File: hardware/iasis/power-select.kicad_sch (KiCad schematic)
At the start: 23 parts, among them Q1911 2N7002, Q1912 2N7002, U1901 AP22653W6-7, U1902 TPS259470LRPWR

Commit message: Wire the schematic islands and side-match the RP2354 GPIOs
Each sheet now draws its circuits with wires. Labels remain at block edges
and on single-part islands: buttons, test points, decoupling and pull
resistors. The target-port page wires its hierarchical labels straight to
the child sheet pins, the ports page points its labels away from each
block, and the root sheet keeps every block clear of the title block.

The RP2354B GPIOs are reassigned so each signal leaves the package on the
side facing its destination. Update PCB from Schematic applied the 43
U1101 pad-net changes with no geometry change. Otherwise the netlist
matches the previous design, ERC keeps its 14 existing warnings and DRC
reports no parity issues.
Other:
- moved on the sheet: C1903, C1904, C1905, C1906, C1911, C1912, C1913, Q1911, Q1912, R1906, R1907, R1908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

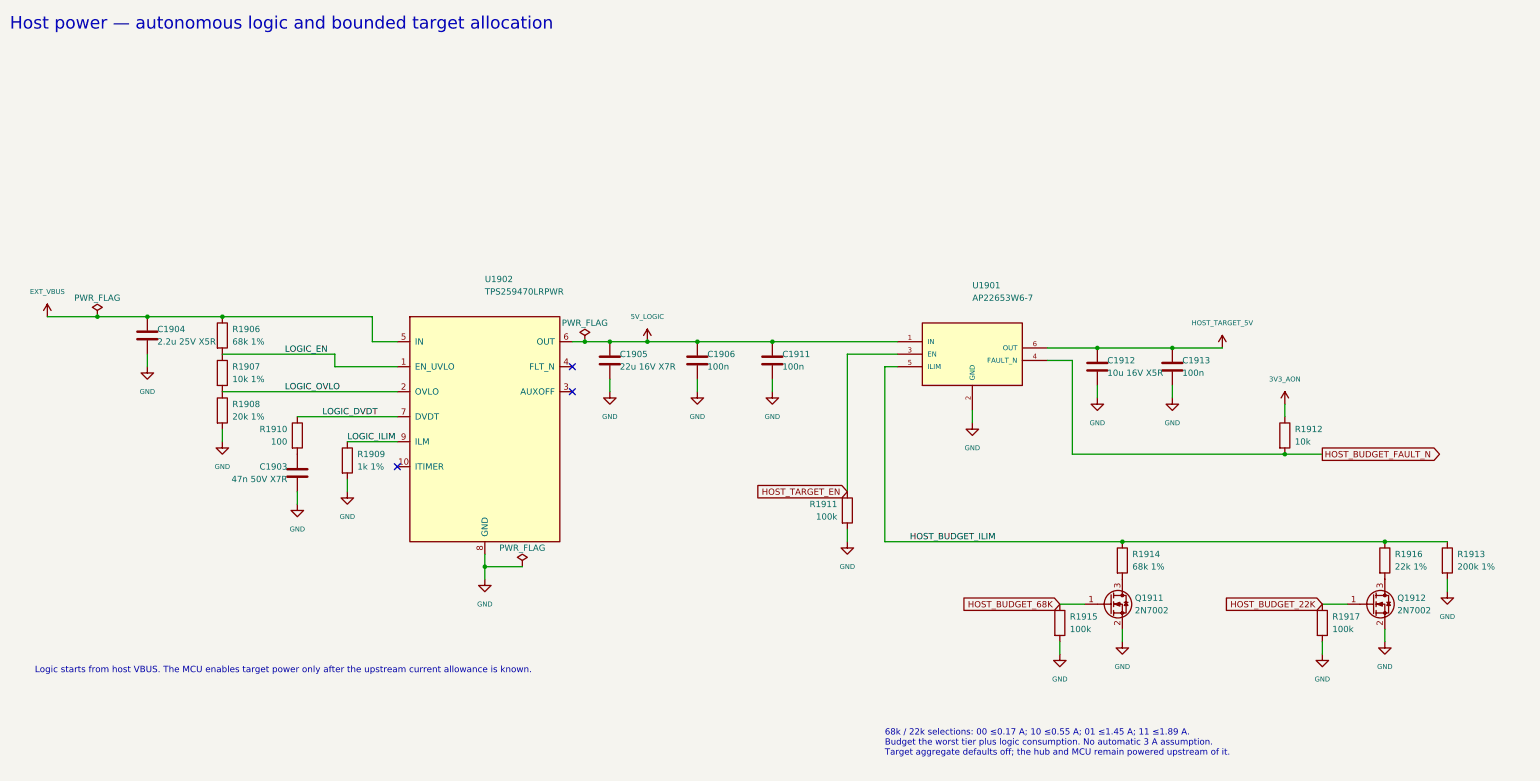
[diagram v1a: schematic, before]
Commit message: Redraw the power input, host power and logic supply sheets
The charging input, host power budget and logic supply sheets follow
the power path left to right: connector and protection, switches and
eFuses, then the converters with their feedback and output capacitors.
Supply rails use power symbols with their existing net names, notes sit
beside their circuits, and each sheet carries a title, date and
revision. The netlist is unchanged.
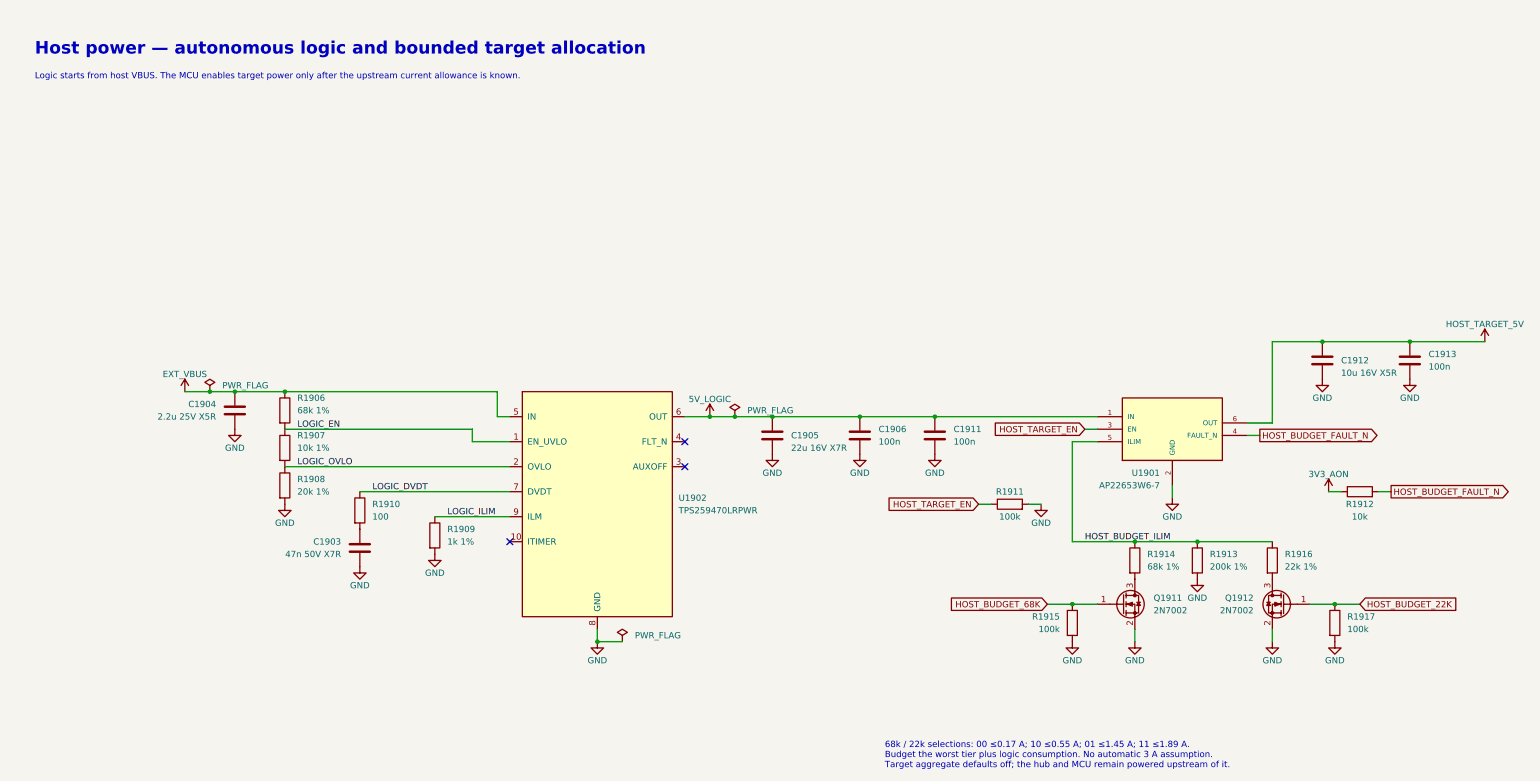
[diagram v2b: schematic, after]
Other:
- title: (none) -> Host power and target budget
- moved on the sheet: C1903, C1904, C1905, C1906, C1911, C1912, C1913, Q1911, Q1912, R1906, R1907, R1908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

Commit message: fix: correct core power and recovery circuitry
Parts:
- R1906: value 68k 1% -> 64.9k 0.1%; LCSC C36871 -> C852880; MPN 0402WGF6802TCE -> RT0402BRD0764K9L; Manufacturer UNI-ROYAL(Uniroyal Elec) -> YAGEO
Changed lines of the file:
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@@
 			)
 		)
-		(property "Value" "68k 1%"
+		(property "Value" "64.9k 0.1%"
 			(at 78.74 95.25 0)
 			(show_name no)
@@
 			)
 		)
-		(property "Datasheet" "https://www.lcsc.com/datasheet/lcsc_datasheet_2206010030_UNI-ROYAL-Uniroyal-Elec-0402WGF6802TCE_C36871.pdf"
+		(property "Datasheet" "https://www.yageogroup.com/component-documentation/download/specsheet/RT0402BRD0764K9L"
 			(at 78.74 95.25 0)
 			(hide yes)
@@
 			)
 		)
-		(property "LCSC" "C36871"
+		(property "LCSC" "C852880"
 			(at 76.2 95.25 0)
 			(hide yes)
@@
 			)
 		)
-		(property "MPN" "0402WGF6802TCE"
+		(property "MPN" "RT0402BRD0764K9L"
 			(at 76.2 95.25 0)
 			(hide yes)
@@
 			)
 		)
-		(property "Manufacturer" "UNI-ROYAL(Uniroyal Elec)"
+		(property "Manufacturer" "YAGEO"
 			(at 76.2 95.25 0)
 			(hide yes)
